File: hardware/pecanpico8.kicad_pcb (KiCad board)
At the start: 4 copper layers, 29.8 x 44.7 mm, 145 parts, among them IC1 SPV1040, IC2 TPS62260, IC3 ADP322ACPZ-115-R7, IC4 Si4464, IC5 STM32F745IGKx, IC6 EVA-7M, IC7 PAC1720, IC8 LDLN015PU30R, IC9 BME280, P1 CONN_02X13, P2 CONN_01X11, P3 ZX62-B-5PA(33), P4 IPX 2mm, P5 CONN_01X02, P6 IPX 2mm, P7 CONN_02X13, Q1 FDN306P, U3 uctronics OV2640, X1 KT2016K26000BCW18ZAS

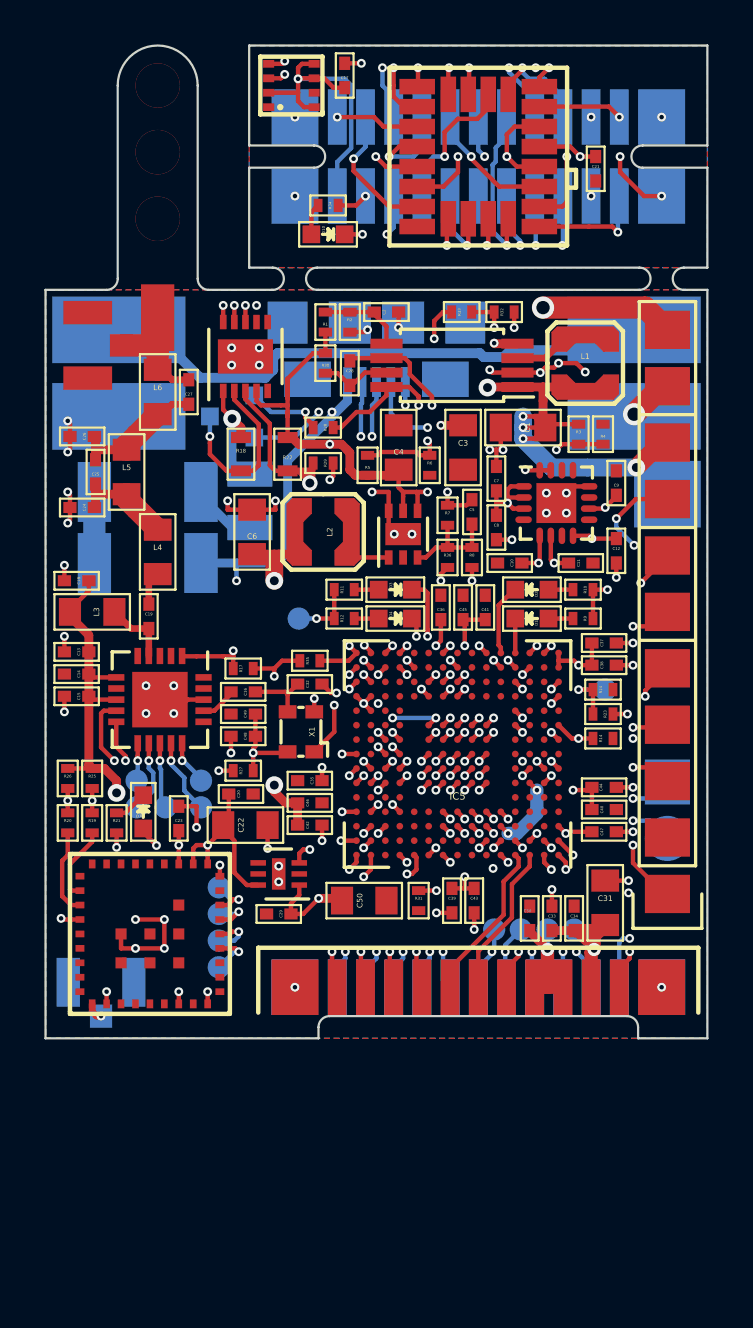
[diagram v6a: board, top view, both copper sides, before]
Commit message: Replaced inductor for SPV1040, added production information, created GERBERs
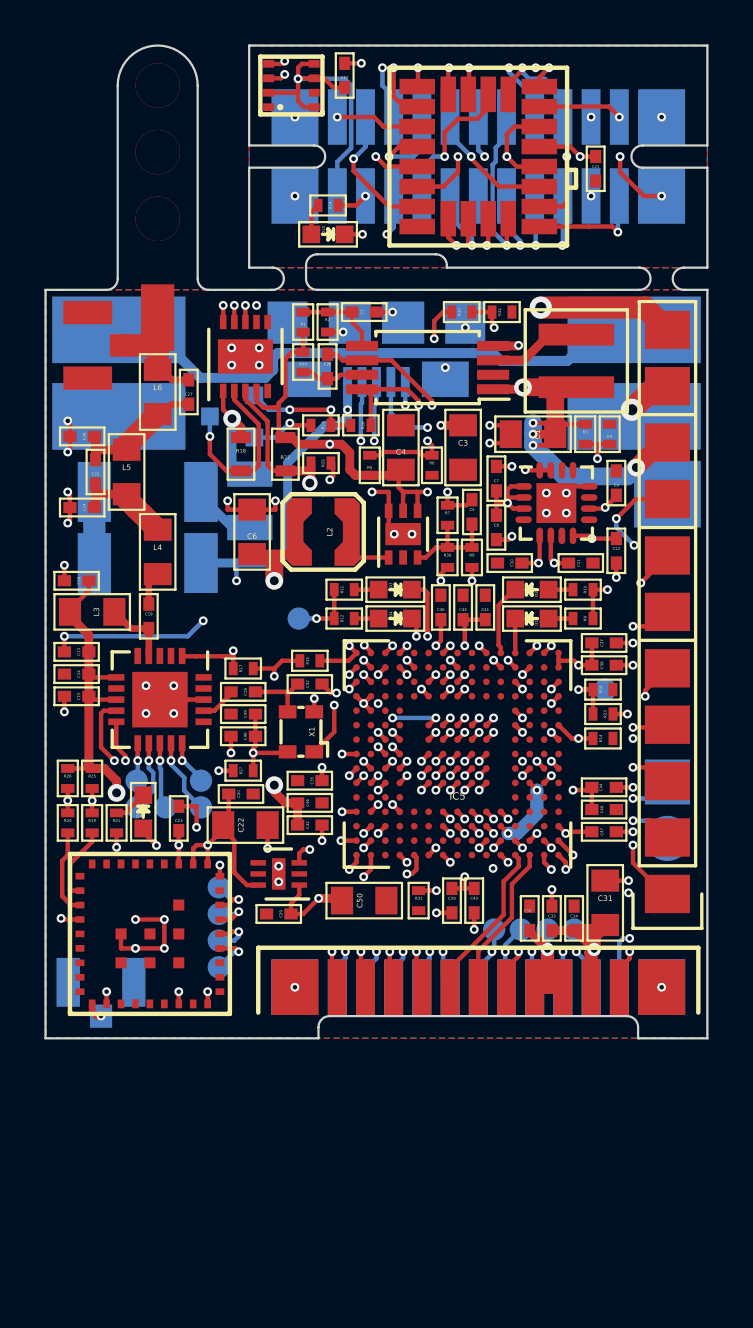
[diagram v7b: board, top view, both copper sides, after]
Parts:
- added R13: N/A, stm32f7:R_0402, F.Cu at (59.5, 97.0)
- C28: value ? -> 1u
- D8, D9: value DIODE -> RFN1L7STE25
- F1: value 500mA -> PMS1206-075
- IC1: value SPV1040 -> SPV1040T
- IC2: value TPS62260 -> TPS62260DRVR
- IC4: value Si4464 -> Si4063-B1B-FM
- IC5: value STM32F745IGKx -> STM32F429IIH6
- IC7: value PAC1720 -> PAC1720-1-AIA-TR
- IC8: value LDLN015PU30R -> LDLN015PU33R
- L1: value 10u -> XAL4040-103; footprint stm32f7:LPS3015 -> stm32f7:XAL4040
- L2: value 2u2 -> LPS3015-222
- R10, R11, R12, R9: value 0R -> 1k5
- R19, R20: value 0R -> N/A
- R21: value 1k -> 1k5
- R29, R30: value ? -> 1k
- R34: value 0R -> 1k
- moved R28 1.70 mm to (61.3, 97.0)
- moved IC1 1.10 mm to (64.3, 94.4)
- moved C28 1.04 mm to (59.8, 94.3)
- moved R30 1.00 mm to (58.7, 94.2)
- moved C2 1.00 mm to (61.5, 91.9)
- moved R1 1.00 mm to (58.7, 92.3)
- moved R2 1.00 mm to (59.8, 92.3)
- moved C1 0.54 mm to (69.0, 97.4)
- moved L1 0.41 mm to (71.0, 94.1)
- moved R3 0.30 mm to (71.4, 97.4)
- moved R4 0.30 mm to (72.5, 97.4)
- moved C4 0.10 mm to (63.1, 98.0)
- moved R22 0.10 mm to (57.9, 98.3)
- moved R29 0.10 mm to (59.5, 98.7)
- moved R5 0.10 mm to (61.7, 98.8)
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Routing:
- net +BATT: track 33.7 -> 29.5 mm
- net +SOL: track 44.3 -> 46.8 mm
- net Net-(IC1-Pad3): track 2.14 -> 4.23 mm
- net GND: track 91.7 -> 93.5 mm, vias 115 -> 114
- net /ADC_VUSB: track 17.9 -> 19.0 mm
- net /OV2640_PWDN: track 15.7 -> 16.4 mm
- net Net-(C28-Pad1): track 12.0 -> 12.6 mm
- net Net-(C28-Pad2): track 3.36 -> 2.85 mm
- net /SOL_SHORT_EN: vias 2 -> 3
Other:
- outline, holes or cut-outs redrawn
- board text added: "April 2017"
- board text removed: "March 2017"

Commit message: Added solder stop opening below QFN vias Removed copper closer than 0.2mm from the edge of the PCB Created new GERBER files
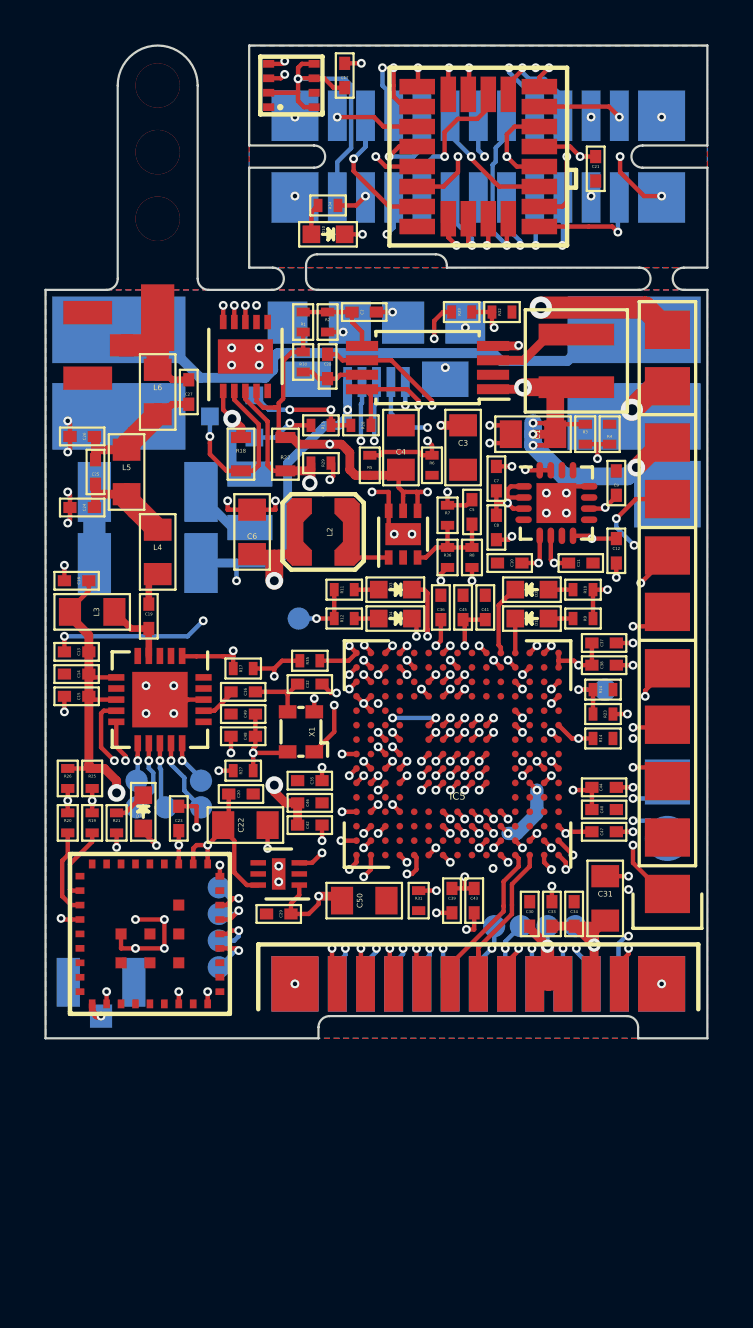
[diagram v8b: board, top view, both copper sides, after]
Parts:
- moved C30 0.20 mm to (68.9, 119.0)
- moved C31 0.20 mm to (72.3, 118.3)
- moved C33 0.20 mm to (69.9, 119.0)
- moved C34 0.20 mm to (70.9, 119.0)
- moved W22 0.16 mm to (71.0, 119.5)
- moved W23 0.15 mm to (69.7, 119.5)
- moved W26 0.15 mm to (67.3, 119.5)
- moved W27 0.15 mm to (68.5, 119.5)
- moved P1 0.15 mm to (66.6, 122.2)
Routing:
- net /CAM_GPIO1: track 6.91 -> 8.38 mm
- net /GPS_EN: track 4.84 -> 3.64 mm
- net VDDA: track 28.3 -> 29.0 mm
- net /CAM_GPIO0: track 7.29 -> 7.99 mm
